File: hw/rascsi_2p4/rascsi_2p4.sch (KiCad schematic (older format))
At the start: 89 parts, among them IC1 SN74LS641-1DW, IC2 SN74LS641-1DW, IC3 SN74LS641-1DW, IC4 SN74LS641-1DW, J1 Raspberry_Pi_2_3, J2 DNP, J4 I2C Pinout, J5 DNP, J6 CONNFLY DB-25, J7 DNP, X1 Mac, X2 Dogcow, X3 Mac, X4 Dogcow, X5 Dogcow, X6 Dogcow, X7 Pi, X8 Pi

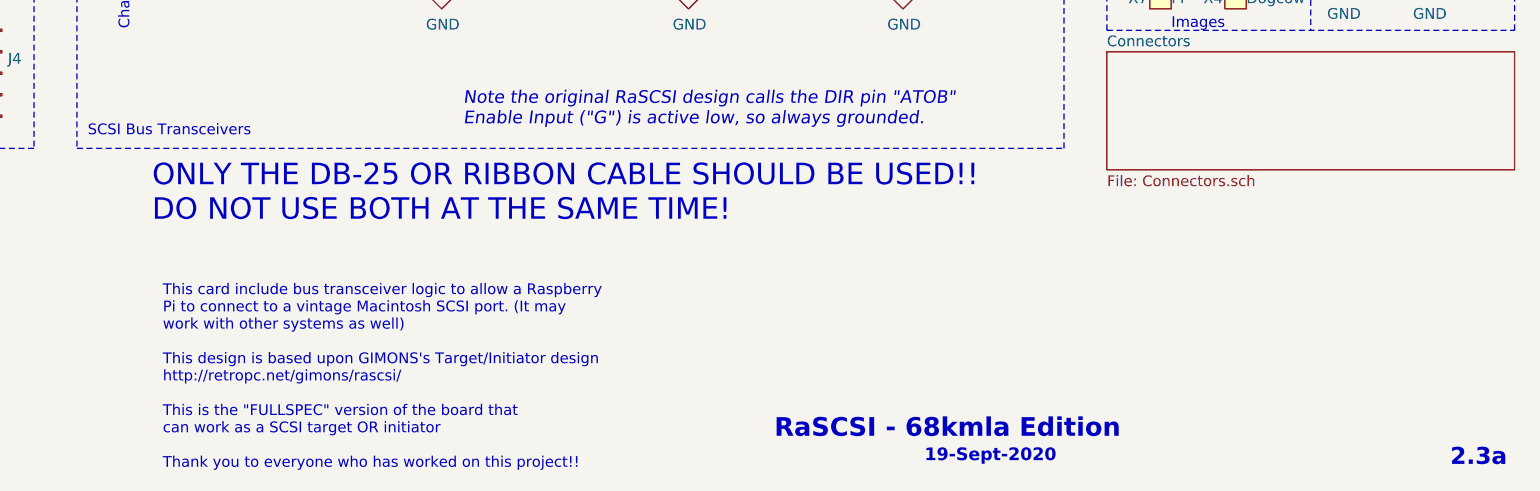
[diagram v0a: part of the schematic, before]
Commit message: Clean up silkscreen and fix DRC issues
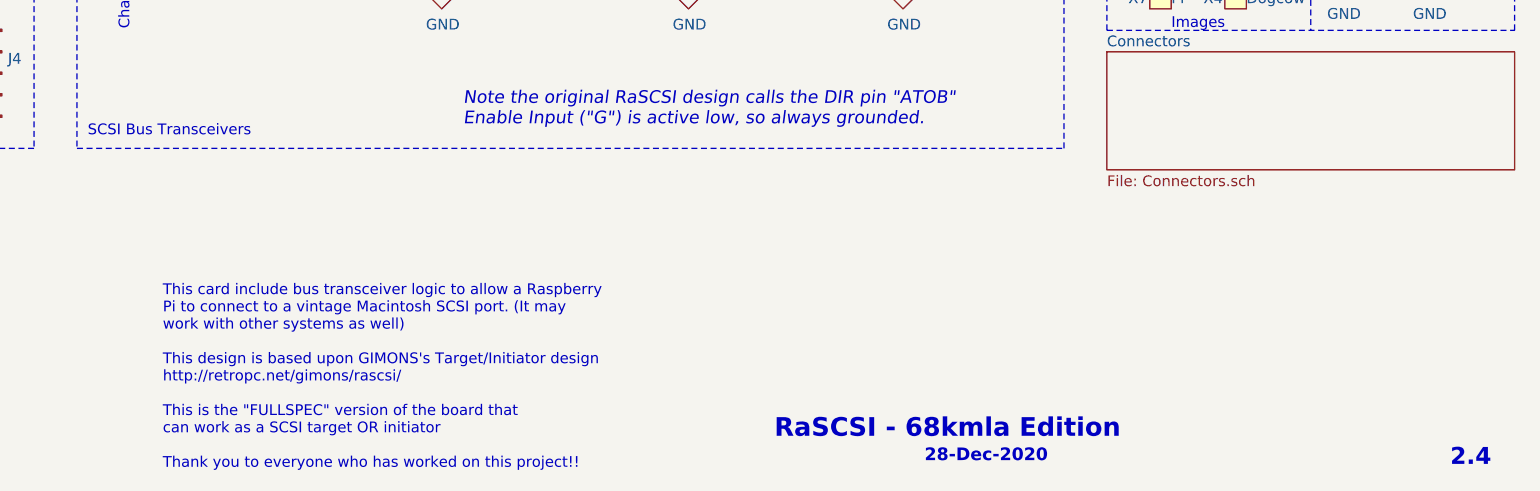
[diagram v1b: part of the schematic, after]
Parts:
- R1, R10, R11, R12, R13, R14, R15, R16, R17, R18, R19, R2, R20, R21, R22, R23, R24, R25, R26, R27, R28, R29, R3, R30, R31, R32, R33, R34, R35, R36, R37, R38, R39, R4, R40, R41, R42, R43, R44, R45, R46, R47, R48, R49, R5, R50, R51, R52, R53, R54, R55, R56, R57, R58, R6, R7, R8, R9: footprint Resistor_THT:R_Axial_DIN0204_L3.6mm_D1.6mm_P1.90mm_Vertical -> Resistor_SMD:R_0402_1005Metric
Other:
- note added: "2.4"
- note added: "28-Dec-2020"
- note removed: "19-Sept-2020"
- note removed: "2.3a"
- note removed: "ONLY THE DB-25 OR RIBBON CABLE SHOULD BE USED!!\nDO NOT USE BOTH AT THE SAME TIME!"
